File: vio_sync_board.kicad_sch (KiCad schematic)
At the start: 8 parts, among them J1 Conn_IMU_Pi_Cam, Q1 BSS138, U1 MCP1700x-180xxTT

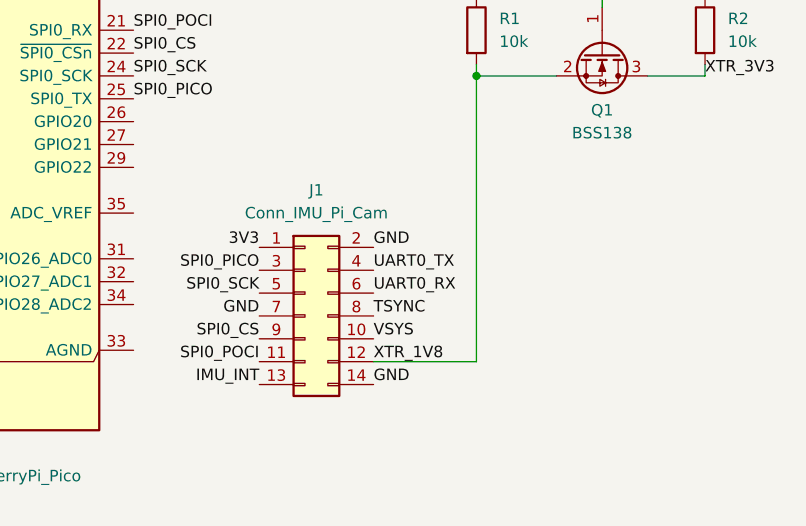
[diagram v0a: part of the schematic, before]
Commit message: refine header and hole position
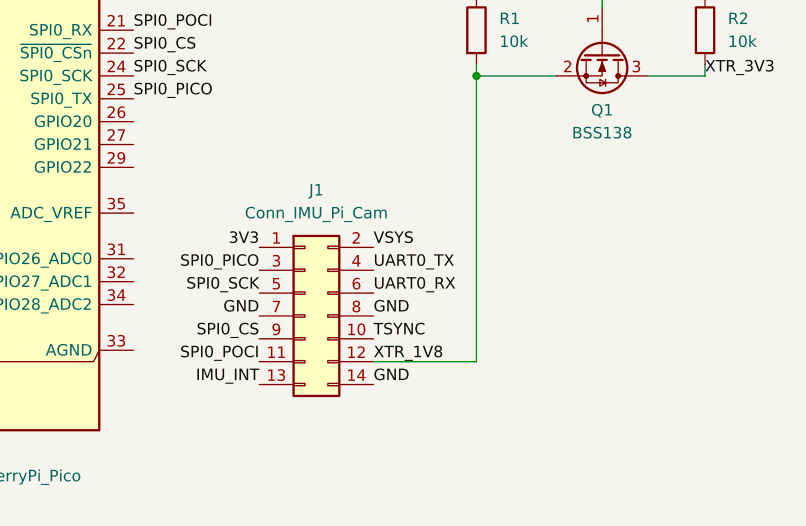
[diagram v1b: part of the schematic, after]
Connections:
- net GND: now also J1.8 (Pin_8); no longer J1.2 (Pin_2)
- net TSYNC: now also J1.10 (Pin_10); no longer J1.8 (Pin_8)
- net VSYS: now also J1.2 (Pin_2); no longer J1.10 (Pin_10)
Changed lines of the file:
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@@
 		)
 	)
-	(label "TSYNC"
+	(label "GND"
 		(at 116.84 90.17 0)
 		(effects
@@
 		)
 	)
-	(label "GND"
+	(label "VSYS"
 		(at 116.84 82.55 0)
 		(effects
@@
 		)
 	)
-	(label "VSYS"
+	(label "TSYNC"
 		(at 116.84 92.71 0)
 		(effects

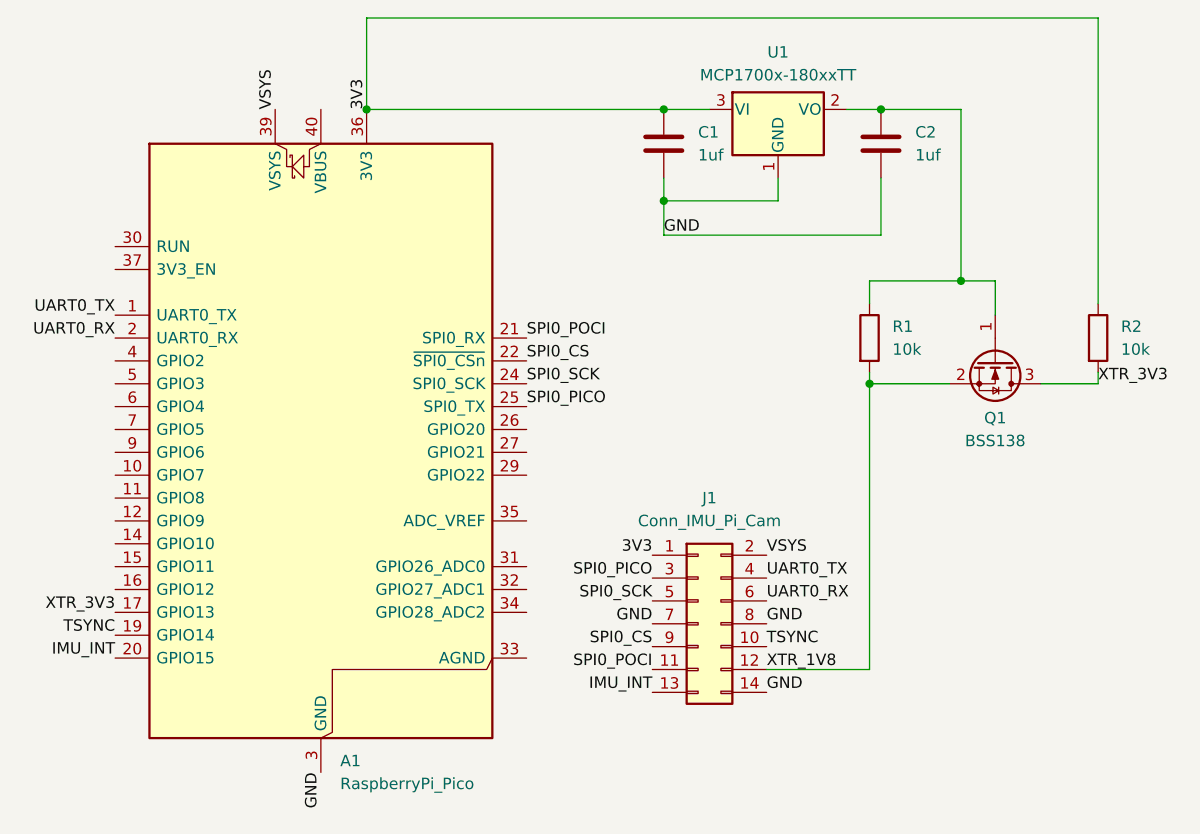
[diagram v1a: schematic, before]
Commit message: DNP pico & header
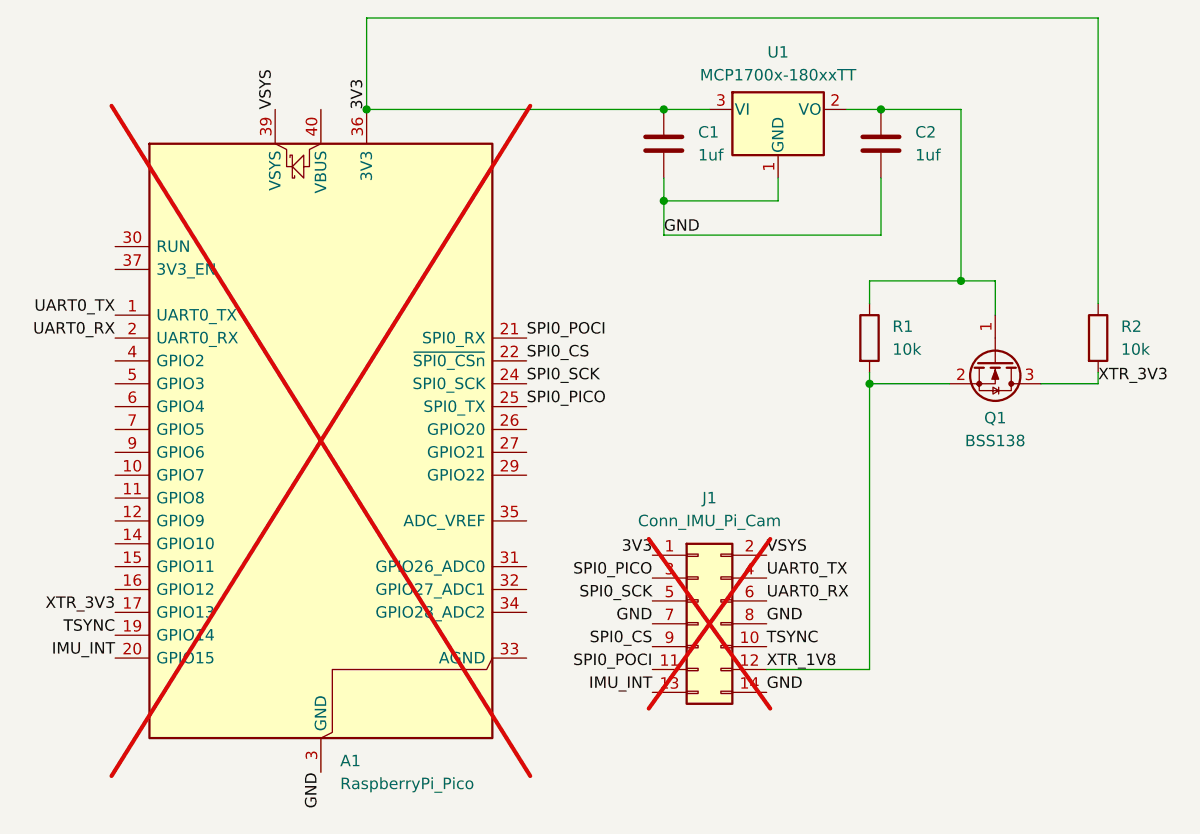
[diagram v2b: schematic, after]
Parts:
- A1, J1: now not fitted; now left out of the parts list
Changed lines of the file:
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@@
 		(unit 1)
 		(exclude_from_sim no)
-		(in_bom yes)
-		(on_board yes)
-		(dnp no)
+		(in_bom no)
+		(on_board yes)
+		(dnp yes)
 		(fields_autoplaced yes)
 		(property "Reference" "A1"
@@
 		(unit 1)
 		(exclude_from_sim no)
-		(in_bom yes)
-		(on_board yes)
-		(dnp no)
+		(in_bom no)
+		(on_board yes)
+		(dnp yes)
 		(fields_autoplaced yes)
 		(property "Reference" "J1"
